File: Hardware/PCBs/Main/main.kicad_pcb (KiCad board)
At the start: 2 copper layers, 73 x 139 mm, 137 parts, among them J2 HARWIN M20, J3 USB4110GFA, J4 F3311A7H121010E200, SW1 EVQQ2P03W, SW10 EVPBT1C4A000, SW11 EVPBT1C4A000, SW12 EVPBT1C4A000, SW13 EVPBT1C4A000, SW14 EVPBT1C4A000, SW15 EVPBT1C4A000, SW16 EVPBT1C4A000, SW17 EVPBT1C4A000, SW18 EVPBT1C4A000, SW19 EVPBT1C4A000, SW2 Nidec CUS-12TB, SW20 EVPBT1C4A000, SW21 EVPBT1C4A000, SW22 EVPBT1C4A000, SW23 EVPBT1C4A000, SW24 EVPBT1C4A000, SW25 EVPBT1C4A000, SW26 EVPBT1C4A000, SW27 EVPBT1C4A000, SW28 EVPBT1C4A000, SW29 EVPBT1C4A000, SW3 EVPBT1C4A000, SW30 EVPBT1C4A000, SW31 EVPBT1C4A000, SW32 EVPBT1C4A000, SW33 EVPBT1C4A000, SW34 EVPBT1C4A000, SW35 EVPBT1C4A000, SW36 EVPBT1C4A000, SW37 EVPBT1C4A000, SW38 EVPBT1C4A000, SW39 EVPBT1C4A000, SW4 EVPBT1C4A000, SW40 EVPBT1C4A000, SW41 EVPBT1C4A000, SW42 EVPBT1C4A000, SW43 EVPBT1C4A000, SW44 EVPBT1C4A000, SW45 EVPBT1C4A000, SW46 EVPBT1C4A000, SW47 EVPBT1C4A000, SW48 EVPBT1C4A000, SW49 EVPBT1C4A000, SW5 EVPBT1C4A000, SW50 EVPBT1C4A000, SW51 EVPBT1C4A000, SW6 EVPBT1C4A000, SW7 EVPBT1C4A000, SW8 EVPBT1C4A000, SW9 EVPBT1C4A000, U1 STM32U385RGT6Q, U2 TPS61299, U3 MX25R6435FM2IL0, U4 TLV73333PDBVR, U5 LM66100QDCKRQ1, U6 LM66100QDCKRQ1, U7 NBM5100A, Y1 32768 Hz

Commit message: Update rev 4 schematics
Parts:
- added JP1: Bootloader, Resistor_SMD:R_0603_1608Metric_Pad0.98x0.95mm_HandSolder, F.Cu at (87.1, 43.9)
- added R29: 33, Resistor_SMD:R_0603_1608Metric_Pad0.98x0.95mm_HandSolder, F.Cu at (98.2, 54.3)
- added R30: 33, Resistor_SMD:R_0603_1608Metric_Pad0.98x0.95mm_HandSolder, F.Cu at (105.4, 53.3)
- added R31: 0, Resistor_SMD:R_0603_1608Metric_Pad0.98x0.95mm_HandSolder, F.Cu at (92.2, 70.6)
- R25: value 100 -> 0
- moved R24 5.10 mm to (102.3, 54.3)
- moved R20 3.90 mm to (96.2, 54.3)
- moved R21 2.50 mm to (100.3, 54.3)
- moved D2 0.67 mm to (105.7, 55.3)
- moved R19 0.20 mm to (94.1, 54.3)
- renumbered TP8 to +5V, TP1 to 5VEN, TP2 to DISP, TP9 to GND, TP6 to SCLK, TP5 to SCS, TP4 to SI, TP12 to USBON, TP13 to VCAP, TP11 to VCH, TP7 to VDD, TP10 to VIN, TP3 to XTCOMIN
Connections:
- J3 pad A8: unconnected-(J3-SBU1-PadA8) -> Net-(J3-SBU1)
- J3 pad B8: unconnected-(J3-SUB2-PadB8) -> Net-(J3-SUB2)
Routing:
- net /SWDIO: track 31.2 -> 91.3 mm, vias 0 -> 4
- net /SWCLK: track 25.2 -> 61.4 mm, vias 2 -> 3
- net Net-(JP1-B): track 4.94 -> 30.2 mm, vias 0 -> 2
- net VDD: track 192.8 -> 217.7 mm, vias 5 -> 8
- net /kh2: track 165.7 -> 181.9 mm
- net /D+: track 30.7 -> 45.8 mm
- net Net-(J3-SBU1): track 0.00 -> 13.9 mm
- net /SI: track 32.4 -> 20.3 mm
- net Net-(D3-A): track 68.3 -> 80.0 mm, vias 4 -> 3
- net GND: track 371.3 -> 359.8 mm, vias 2 -> 0
- net /F_CS: track 43.2 -> 32.7 mm
- net /USB_ON: track 46.3 -> 55.8 mm
- net /SCLK: track 40.1 -> 49.2 mm
- net /kv4: track 177.9 -> 170.0 mm, vias 10 -> 9
- net Net-(J3-CC1): track 14.1 -> 6.17 mm
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
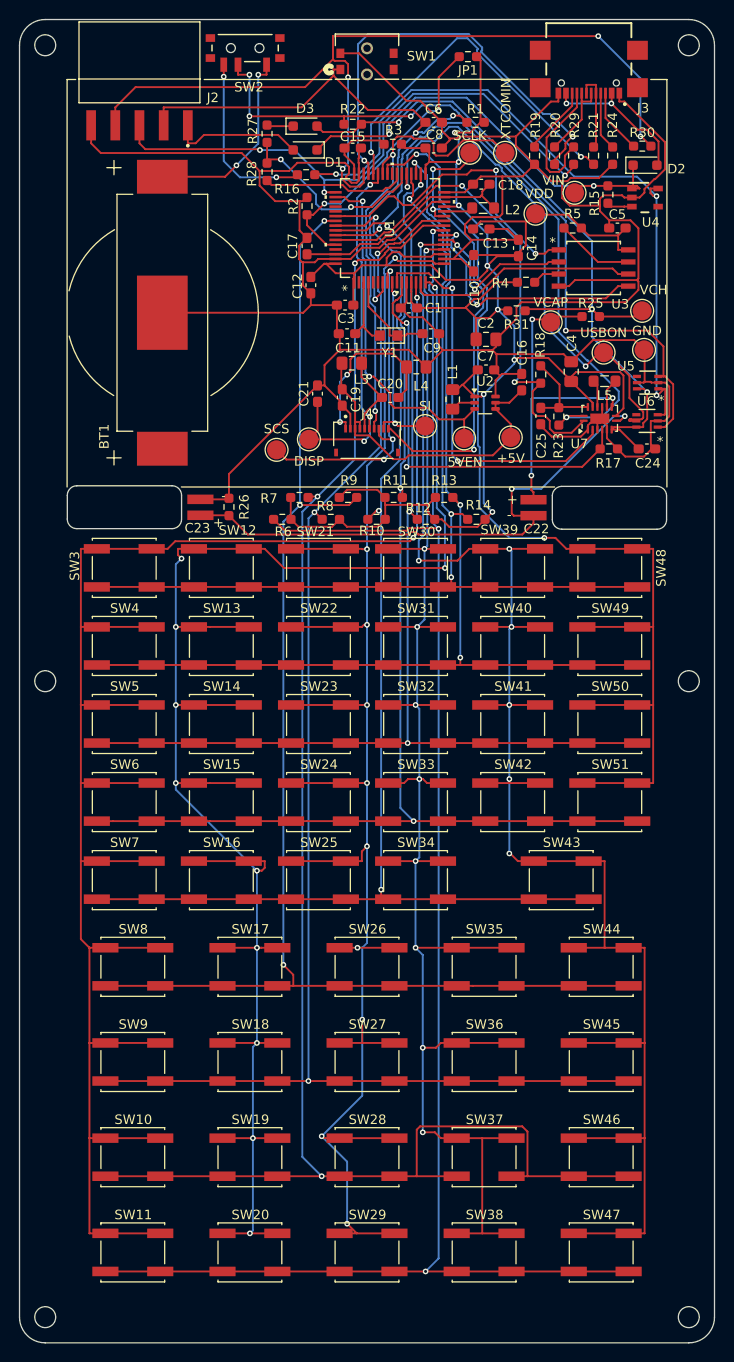
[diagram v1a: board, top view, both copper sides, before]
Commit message: Update component names in schematic, add PDBs
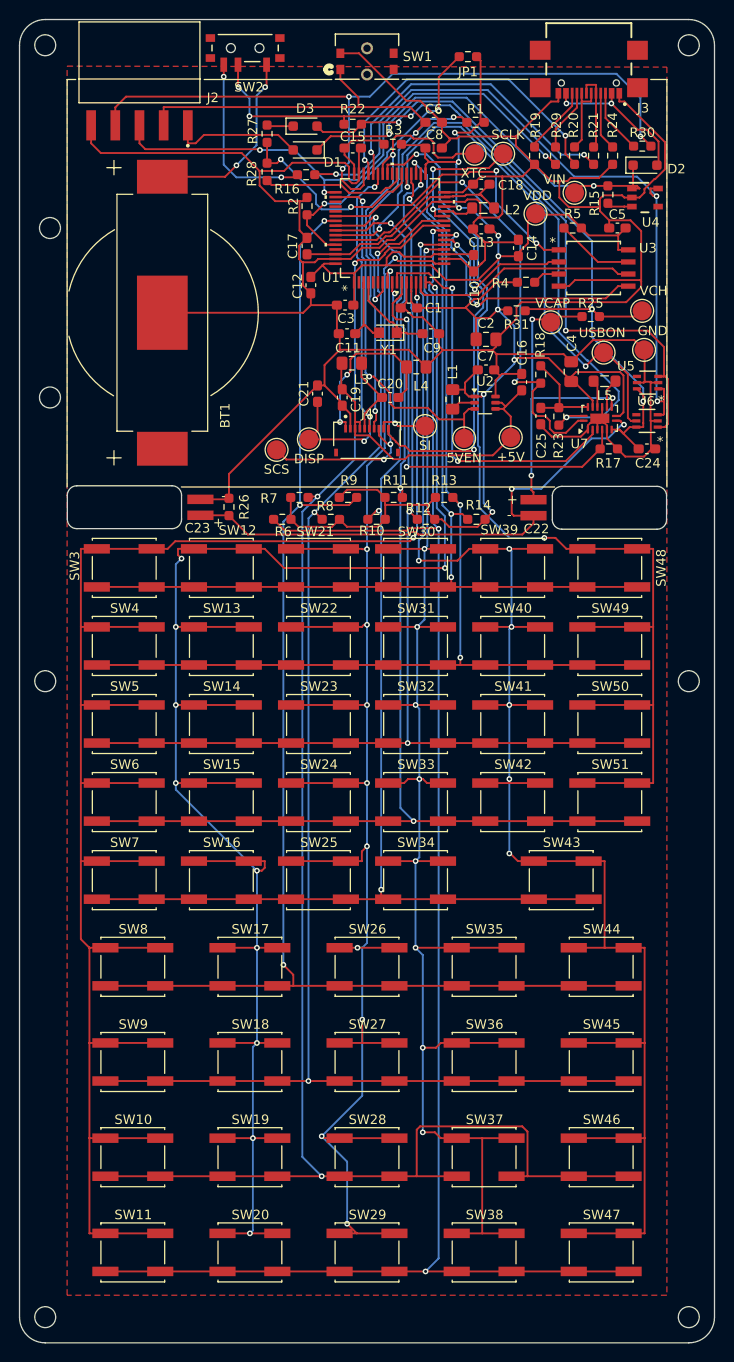
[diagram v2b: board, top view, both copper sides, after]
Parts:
- C24, C25: value 2 uF -> 2.2 uF
- J2: value HARWIN M20 -> HARWIN M20-8890545R
- J3: value USB4110GFA -> USB4110-GF-A
- SW1: value EVQQ2P03W -> TL1014BF160QG
- SW2: value Nidec CUS-12TB -> CUS-12TB
- TP1: renamed from 5VEN; footprint TestPoint:TestPoint_Pad_D2.0mm -> footprints:TestPoint_Pad_D2.0mm
- TP10: renamed from VIN; footprint TestPoint:TestPoint_Pad_D2.0mm -> footprints:TestPoint_Pad_D2.0mm
- TP11: renamed from VCH; footprint TestPoint:TestPoint_Pad_D2.0mm -> footprints:TestPoint_Pad_D2.0mm
- TP12: renamed from USBON; footprint TestPoint:TestPoint_Pad_D2.0mm -> footprints:TestPoint_Pad_D2.0mm
- TP13: renamed from VCAP; footprint TestPoint:TestPoint_Pad_D2.0mm -> footprints:TestPoint_Pad_D2.0mm
- TP2: renamed from DISP; footprint TestPoint:TestPoint_Pad_D2.0mm -> footprints:TestPoint_Pad_D2.0mm
- TP3: renamed from XTCOMIN; footprint TestPoint:TestPoint_Pad_D2.0mm -> footprints:TestPoint_Pad_D2.0mm
- TP4: renamed from SI; footprint TestPoint:TestPoint_Pad_D2.0mm -> footprints:TestPoint_Pad_D2.0mm
- TP5: renamed from SCS; footprint TestPoint:TestPoint_Pad_D2.0mm -> footprints:TestPoint_Pad_D2.0mm
- TP6: renamed from SCLK; footprint TestPoint:TestPoint_Pad_D2.0mm -> footprints:TestPoint_Pad_D2.0mm
- TP7: renamed from VDD; footprint TestPoint:TestPoint_Pad_D2.0mm -> footprints:TestPoint_Pad_D2.0mm
- TP8: renamed from +5V; footprint TestPoint:TestPoint_Pad_D2.0mm -> footprints:TestPoint_Pad_D2.0mm
- TP9: renamed from GND; footprint TestPoint:TestPoint_Pad_D2.0mm -> footprints:TestPoint_Pad_D2.0mm
- U2: value TPS61299 -> TPS61299DRLR
- moved TP6 3.50 mm to (90.8, 54.1)
- moved TP3 3.20 mm to (87.8, 54.1)
- moved R20 2.10 mm to (98.3, 54.3)
- moved R29 1.90 mm to (96.3, 54.3)
- moved Y1 0.31 mm to (78.7, 72.9)
- turned C13 to 0 degrees
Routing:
- net /SWDIO: track 91.3 -> 78.3 mm, vias 4 -> 3
- net /D+: track 45.8 -> 34.4 mm
- net Net-(J3-SBU1): track 13.9 -> 6.55 mm
- net VDD: track 217.7 -> 210.4 mm, vias 8 -> 9
- net /D-: track 38.4 -> 33.9 mm
- net /EXTCOMIN: track 49.2 -> 45.2 mm
- net /SCLK: track 49.2 -> 52.6 mm
- net GND: track 359.8 -> 356.8 mm
- net /SWCLK: track 61.4 -> 58.4 mm
- net /USB_ON: track 55.8 -> 53.0 mm
- net /kv3: track 181.8 -> 179.4 mm
- net Net-(D3-A): track 80.0 -> 78.2 mm
- net /F_CS: track 32.7 -> 30.9 mm
- net Net-(U7-BAL): track 58.7 -> 57.1 mm
- net /kh9: track 104.6 -> 103.4 mm
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- added copper zone on F.Cu, net GND
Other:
- outline, holes or cut-outs redrawn
- board text added: "Rev. 4.0"
- board text added: "https://github.com/apoluekt/OpenRPNCalc"

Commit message: Update battery holder part name
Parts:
- BT1: value BK-5067 -> BC-2013

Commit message: Bugfix 4.0; added HP48 layout
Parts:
- D1, D2, D3: footprint Diode_SMD:D_SOD-323_HandSoldering -> Diode_SMD:D_0603_1608Metric_Pad1.05x0.95mm_HandSolder
- U2: footprint Package_TO_SOT_SMD:Texas_R-PDSO-G6 -> Package_TO_SOT_SMD:SOT-563
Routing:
- net VDD: track 210.4 -> 211.7 mm
- net +5V: track 35.3 -> 36.2 mm
- net GND: track 356.8 -> 357.3 mm
